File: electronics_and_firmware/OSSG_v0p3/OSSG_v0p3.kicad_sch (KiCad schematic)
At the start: 76 parts, among them IC1 DW01A, J1 USB_B_Micro, J2 External PDM Mic Input, Q1 FS8205A, Q2 Q_NPN_BEC, Q3 Q_NPN_BEC, SW1 SW_SPST, U1 ESP32-PICO-D4, U2 TP4056, U3 XC6222B331MRG, U5 APX803L-29SA-7, U6 MP23DB01HPTR

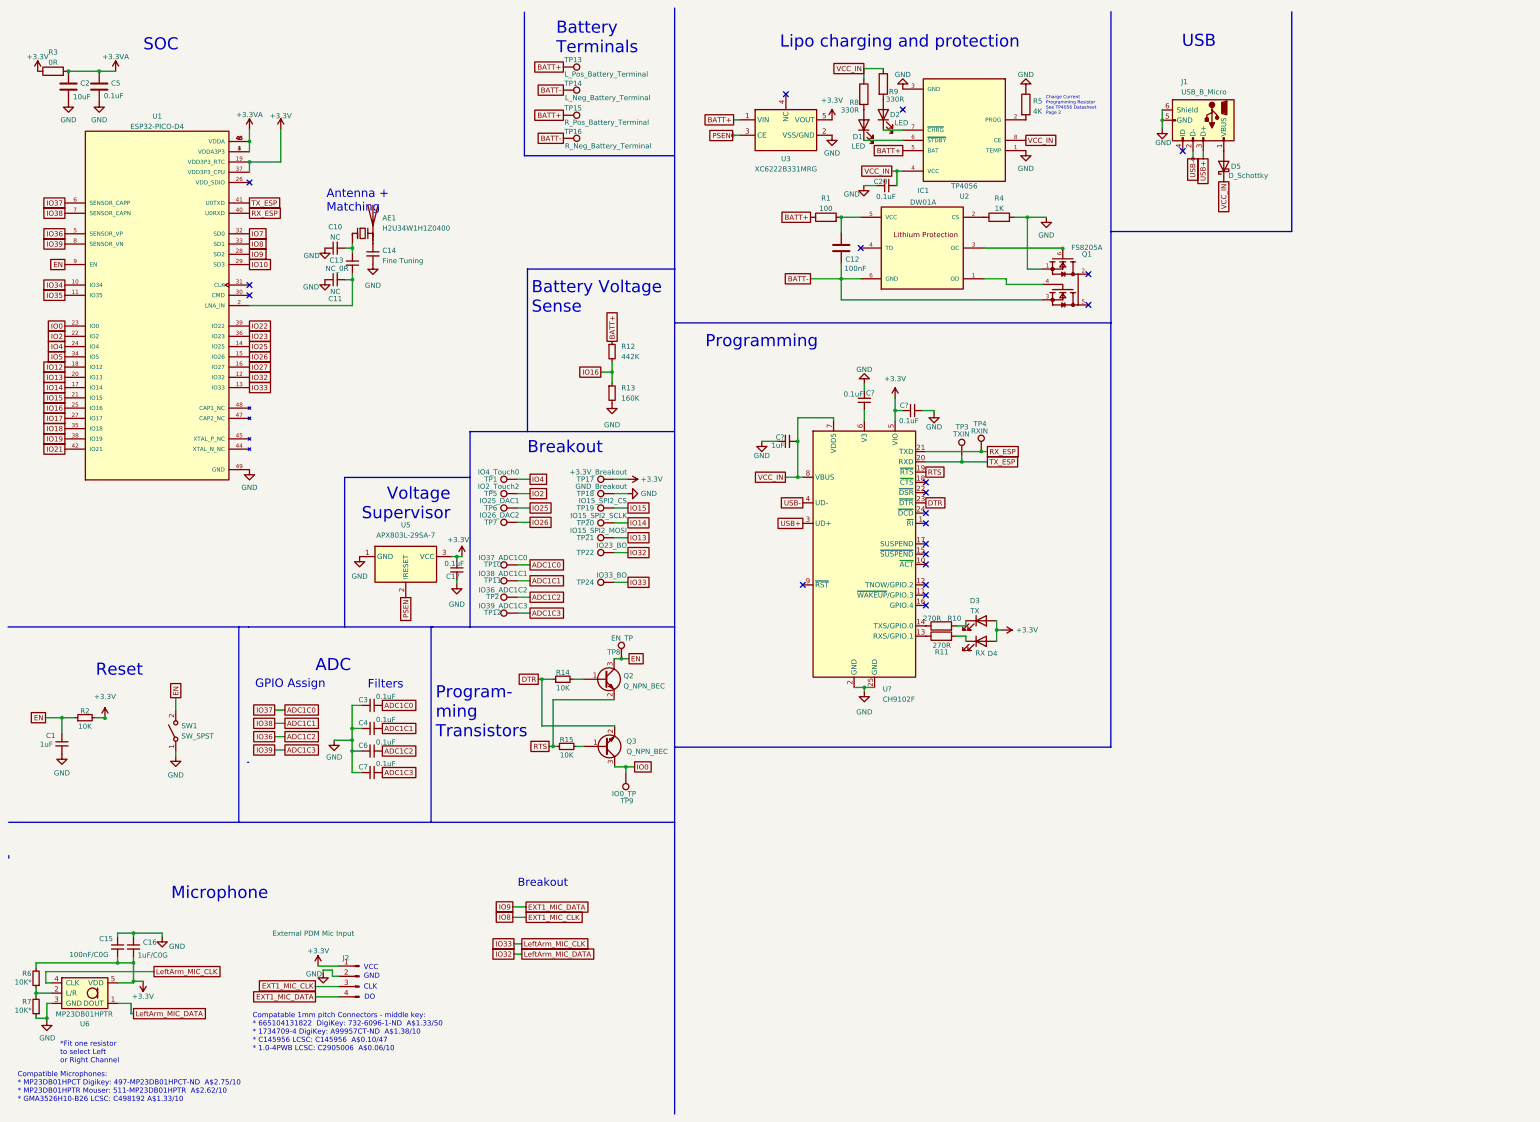
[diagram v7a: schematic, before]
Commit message: add power supply switching, update all footprint to be accurate, move antenna to LCSC part, start new layout
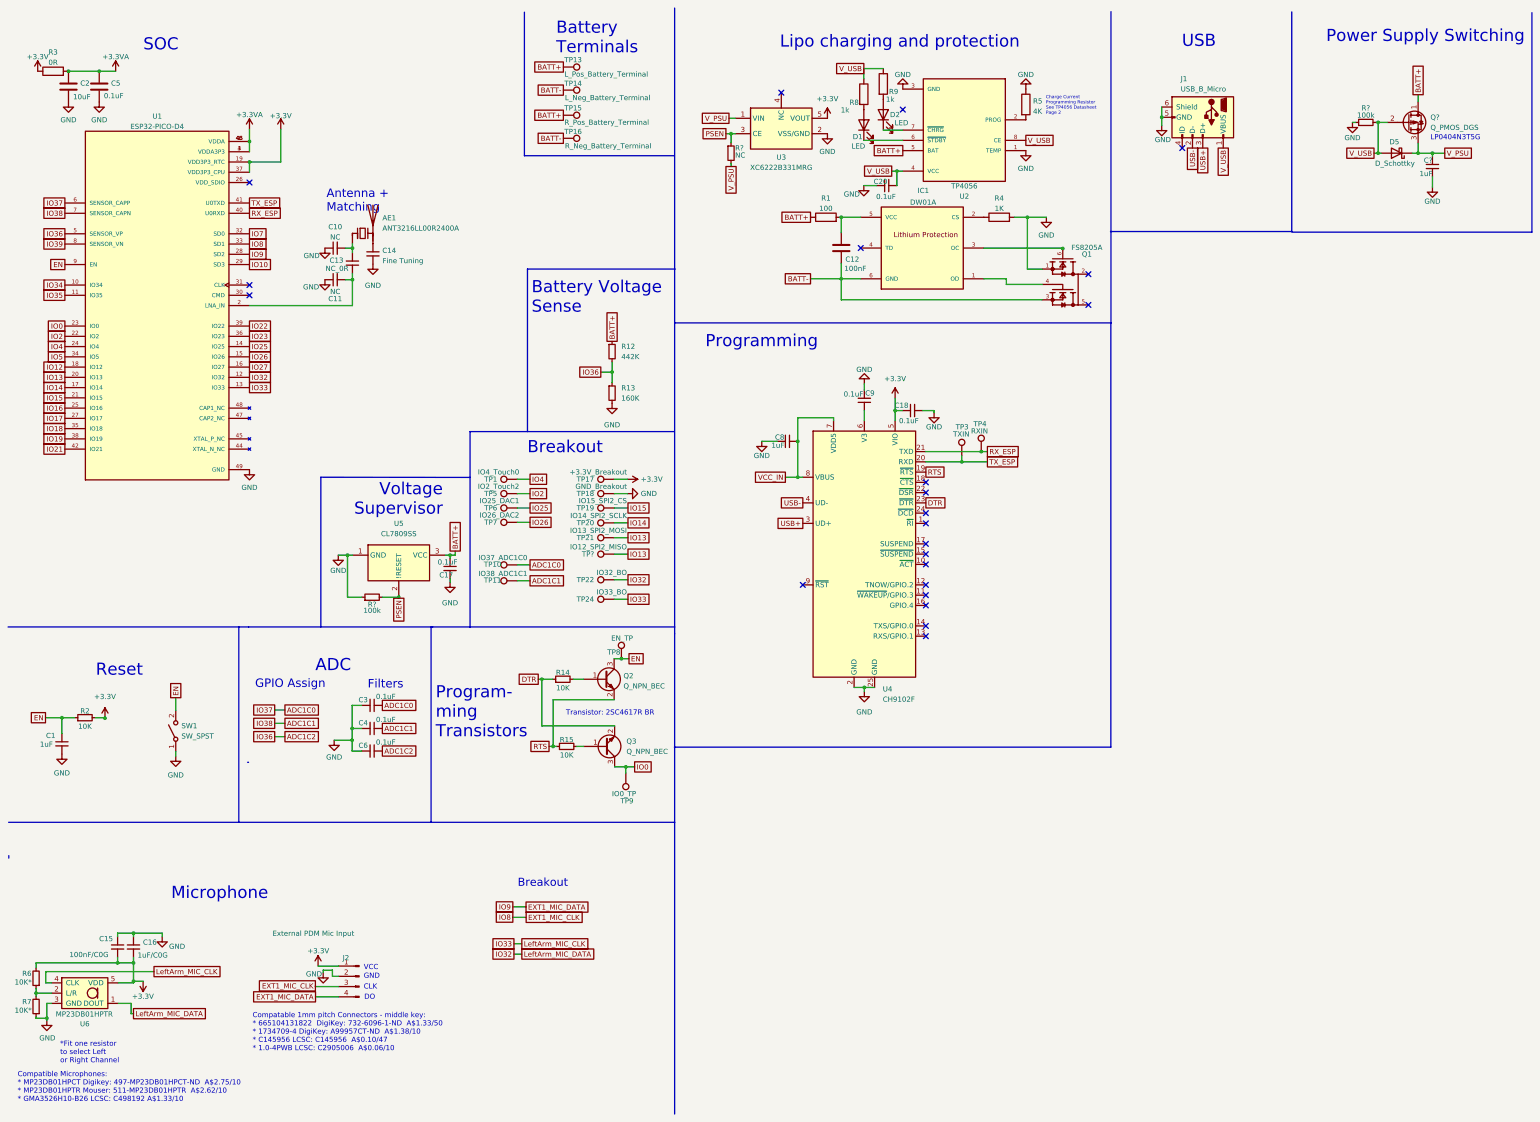
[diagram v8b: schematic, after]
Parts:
- removed C7: 0.1uF, Capacitor_SMD:C_0402_1005Metric, symbol Device:C_Small
- removed D3: TX, Diode_SMD:D_0402_1005Metric, symbol Device:LED
- removed D4: RX, Diode_SMD:D_0402_1005Metric, symbol Device:LED
- removed R10, R11: 270R, Resistor_SMD:R_0402_1005Metric, symbol Device:R
- removed TP12: IO39_ADC1C3, OpenSourceSmartGlasses:BreakoutPadSmall, symbol Connector:TestPoint
- removed TP2: IO36_ADC1C2, OpenSourceSmartGlasses:BreakoutPadSmall, symbol Connector:TestPoint
- added C?: 1uF, Capacitor_SMD:C_0402_1005Metric, symbol Device:C_Small
- added Q?: Q_PMOS_DGS, Package_TO_SOT_SMD:SOT-883, symbol Device:Q_PMOS_DGS
- added R? (x2): 100k, Resistor_SMD:R_0402_1005Metric, symbol Device:R_Small
- added R?: NC, Resistor_SMD:R_0201_0603Metric, symbol Device:R_Small
- added TP?: IO12_SPI2_MISO, OSSG_footprints:Breakout_pads, symbol Connector:TestPoint
- AE1: value H2U34W1H1Z0400 -> ANT3216LL00R2400A; DigiKeyLink https://www.digikey.ca/en/products/detail/unictron-technolo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 -> (none); MPN 2047-H2U34W1H1Z0400CT-ND -> (none); MPN_LCSC None -> C293767; Price 0.9 -> (none); Price_LCSC (none) -> 0.1212
- C10, C11, C13: footprint Capacitor_SMD:C_0402_1005Metric -> Capacitor_SMD:C_0201_0603Metric
- R8, R9: value 330R -> 1k; LCSCLink https://lcsc.com/product-detail/Chip-Resistor-Surface-Mount_YAGEO-RC0402JR-07330RL_C105876.html -> https://lcsc.com/product-detail/Chip-Resistor-Surface-Mount_FOJAN-FRC0402J102-TS_C2906899.html; MPN_LCSC C105876 -> C2906899
- TP1, TP10, TP11, TP13, TP14, TP15, TP16, TP17, TP18, TP19, TP24, TP5, TP6, TP7: footprint OpenSourceSmartGlasses:BreakoutPadSmall -> OSSG_footprints:Breakout_pads
- TP20: value IO15_SPI2_SCLK -> IO14_SPI2_SCLK; footprint OpenSourceSmartGlasses:BreakoutPadSmall -> OSSG_footprints:Breakout_pads
- TP21: value IO15_SPI2_MOSI -> IO13_SPI2_MOSI; footprint OpenSourceSmartGlasses:BreakoutPadSmall -> OSSG_footprints:Breakout_pads
- TP22: value IO23_BO -> IO32_BO; footprint OpenSourceSmartGlasses:BreakoutPadSmall -> OSSG_footprints:Breakout_pads
- U1: footprint OpenSourceSmartGlasses:ESP32_PICO_D4_smallGND -> OSSG_footprints:ESP32_PICO_D4
- U5: value APX803L-29SA-7 -> CL7809SS; DigiKeyLink https://www.digikey.ca/en/products/detail/diodes-incorporat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 -> (none); MPN APX803L-29SA-7DICT-ND -> (none); Price 0.59 -> (none)
- gave numbers to parts that had none: 4
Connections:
- net +3V3: no longer C17.1, U5.3 (VCC)
- net ADC1C2: now also R12.2, R13.1
- net BATT+: now also C17.1, U5.3 (VCC), Q?.1 (D); no longer U3.1 (VIN)
- net GND: now also C?.1, R?.1, R?.1
- net IO13: now also TP?.1
- net IO16: no longer R12.2, R13.1
- net PSEN: now also R?.1, R?.2
- net VCC_IN: no longer C20.1, D5.1 (K), R8.1, R9.1, U2.4 (VCC), U2.8 (CE)
- net V_USB: now reaches D5.2 (A), J1.1 (VBUS)
- net V_USB: now also C20.1, R8.1, R9.1, U2.4 (VCC), U2.8 (CE), Q?.2 (G), R?.2
- net ADC1C3 renamed IO39
- new net V_PSU: C?.2, D5.1 (K), Q?.3 (S), R?.2, U3.1 (VIN)
- no-connect marks 20 -> 22
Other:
- note added: "LP0404N3T5G"
- note added: "Power Supply Switching"
- note added: "Transistor: 2SC4617R BR"
- moved on the sheet: C17, D5, J1, TP22, TP24, U3, U5
